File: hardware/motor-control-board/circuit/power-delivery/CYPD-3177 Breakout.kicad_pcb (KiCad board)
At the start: 2 copper layers, 21.3 x 31.5 mm, 25 parts, among them J1 USB-C Power, J2 Conn_01x12, J4 Conn_01x12, Q1 DMP3013SFV, Q2 DMP3013SFV, U1 CYPD3177

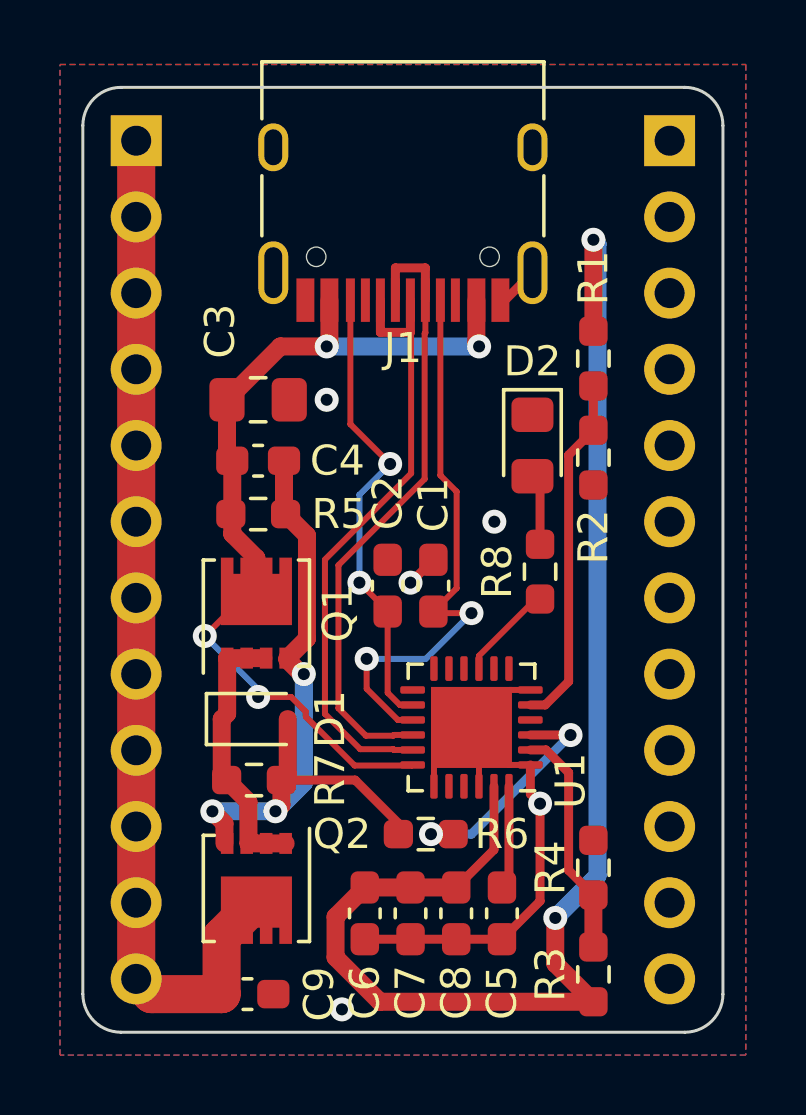
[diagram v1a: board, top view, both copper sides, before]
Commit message: edited USB-C connector footprint to match chosen component - plus other misc DRC fixes - ready for production - some manual adjustment still needed (U1 orientation, USB-C position wrong etc
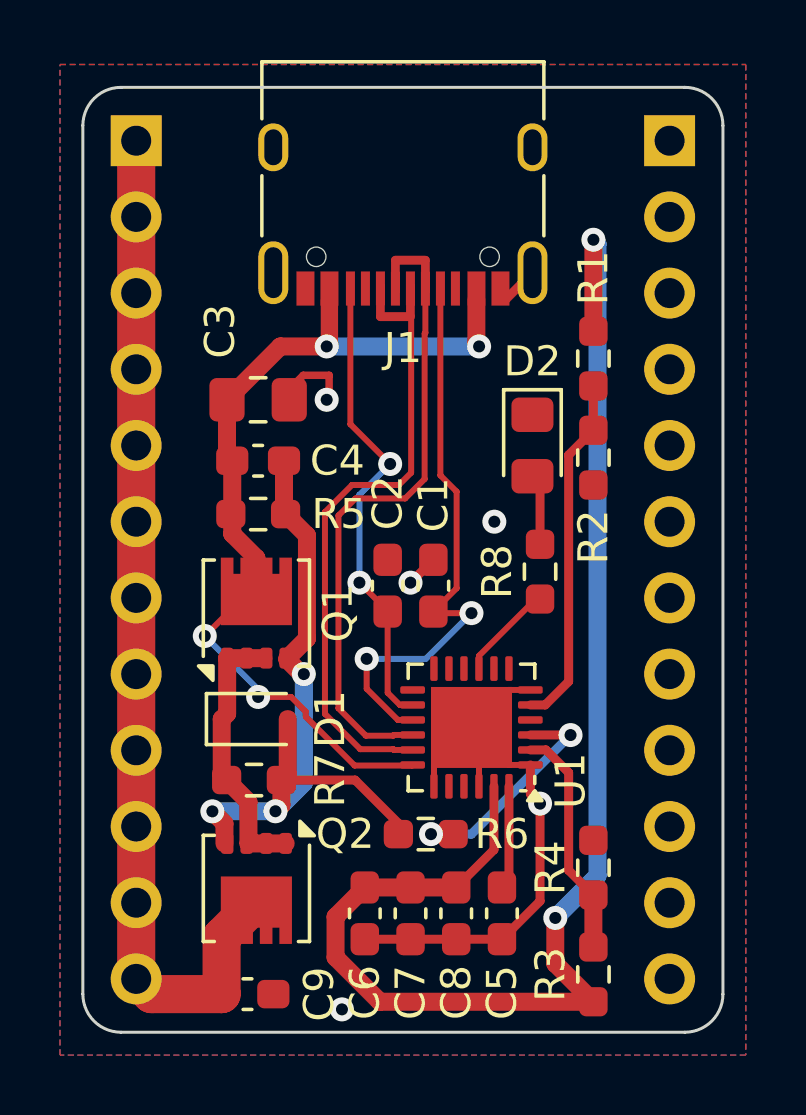
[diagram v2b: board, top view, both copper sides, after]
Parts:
- J1: footprint Connector_USB:USB_C_Receptacle_HRO_TYPE-C-31-M-12 -> Library:SOFNG_MC-311D_12P_Female_USB-C_Connector
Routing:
- net GND: track 23.1 -> 25.8 mm
- net /D-: track 20.8 -> 21.8 mm
- net /D+: track 21.6 -> 22.5 mm
